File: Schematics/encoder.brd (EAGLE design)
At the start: 100 x 80 mm, 2 parts, among them U1 ENCODER_2LED

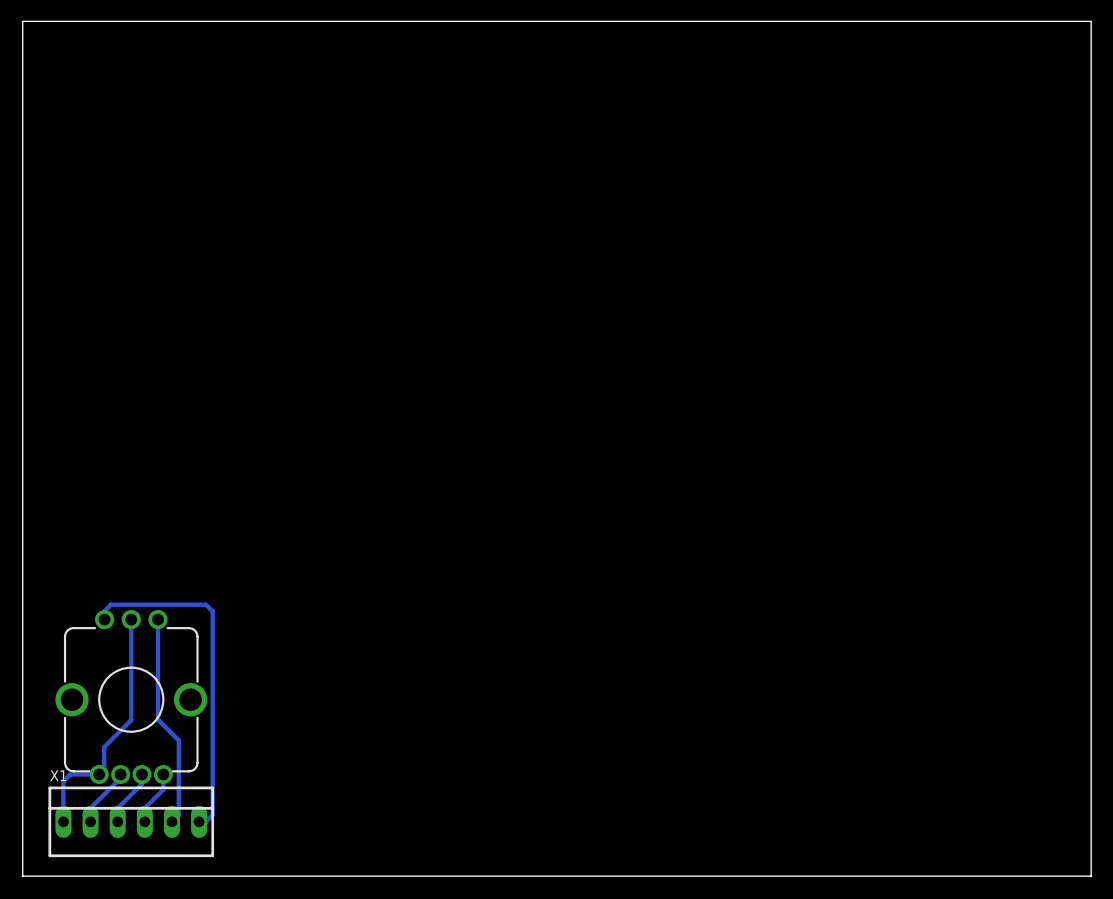
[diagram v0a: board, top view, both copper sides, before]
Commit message: Add caps to encoder breakout
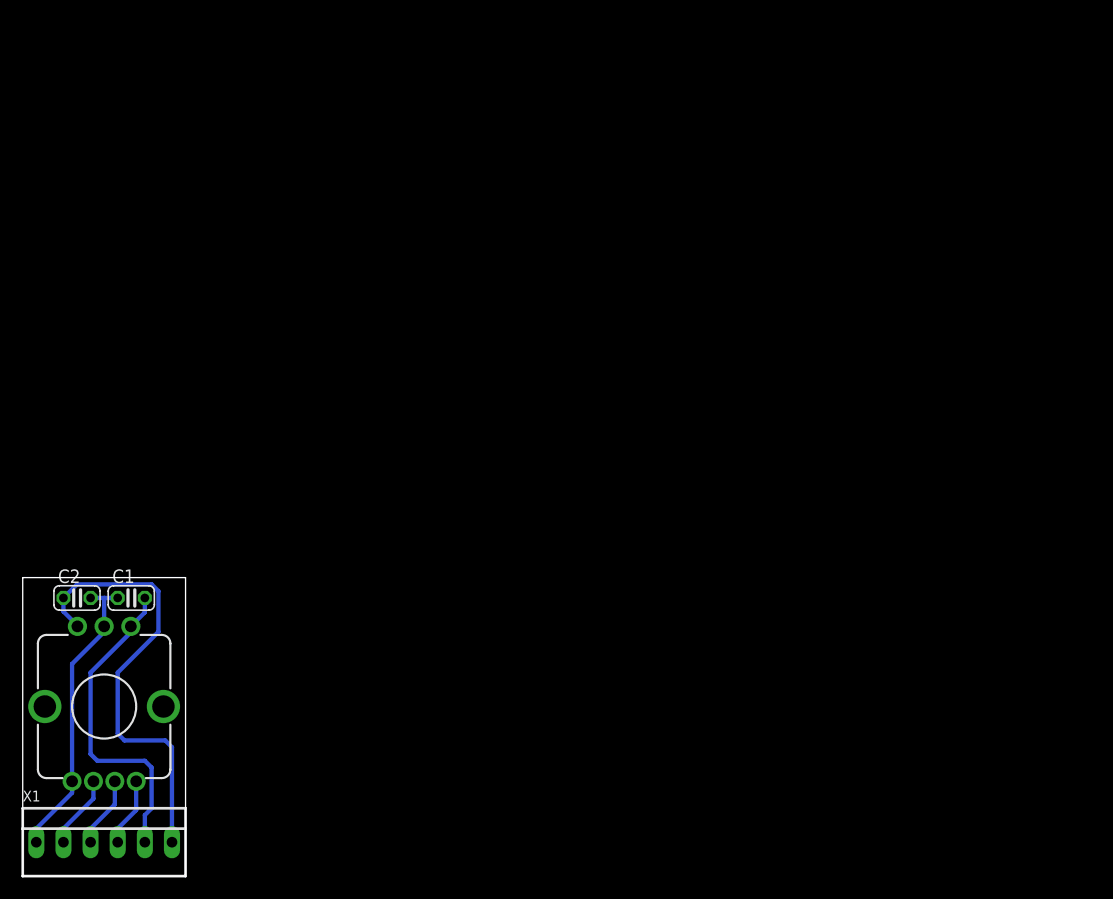
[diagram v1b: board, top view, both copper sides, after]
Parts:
- added C1, C2: (no value), rcl:C025-024X044
- moved X1 3.17 mm to (7.62, 3.17)
- moved U1 2.62 mm to (7.62, 15.9)
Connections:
- removed net N$1: U1.C, U1.GND, X1.1
- new net GND: C1.1, C2.2, U1.C, U1.GND, X1.1
- net N$5: now also C1.2
- net N$6: now also C2.1
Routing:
- net GND: track 0.00 -> 28.0 mm
- net N$1: track 23.2 -> 0.00 mm
- net N$6: track 32.0 -> 42.3 mm
- net N$5: track 20.0 -> 30.2 mm
- net N$3: track 5.37 -> 6.64 mm
- net N$2: track 5.59 -> 6.86 mm
- net N$4: track 5.15 -> 6.42 mm
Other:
- board size 100 x 80 mm -> 15.2 x 27.9 mm
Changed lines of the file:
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@@
 <board>
 <plain>
-<wire x1="0" y1="0" x2="100" y2="0" width="0" layer="20"/>
-<wire x1="100" y1="0" x2="100" y2="80" width="0" layer="20"/>
-<wire x1="100" y1="80" x2="0" y2="80" width="0" layer="20"/>
-<wire x1="0" y1="80" x2="0" y2="0" width="0" layer="20"/>
+<wire x1="0" y1="0" x2="15.24" y2="0" width="0" layer="20"/>
+<wire x1="15.24" y1="0" x2="15.24" y2="27.94" width="0" layer="20"/>
+<wire x1="15.24" y1="27.94" x2="0" y2="27.94" width="0" layer="20"/>
+<wire x1="0" y1="27.94" x2="0" y2="0" width="0" layer="20"/>
 </plain>
 <attributes>
@@
 </autorouter>
 <elements>
-<element name="U1" library="SparkFun" package="ENCODER_LED_2" value="ENCODER_2LED" x="10.16" y="16.51" rot="R180"/>
-<element name="X1" library="con-molex" package="22-23-2061" value="" x="10.16" y="5.08">
-<attribute name="OC_NEWARK" value="27C1933" x="31.75" y="-15.24" size="1.778" layer="27" display="off"/>
-<attribute name="MPN" value="22-23-2061" x="31.75" y="-15.24" size="1.778" layer="27" display="off"/>
-<attribute name="MF" value="MOLEX" x="31.75" y="-15.24" size="1.778" layer="27" display="off"/>
-<attribute name="OC_FARNELL" value="1462922" x="31.75" y="-15.24" size="1.778" layer="27" display="off"/>
+<element name="U1" library="SparkFun" package="ENCODER_LED_2" value="ENCODER_2LED" x="7.62" y="15.875" rot="R180"/>
+<element name="X1" library="con-molex" package="22-23-2061" value="" x="7.62" y="3.175">
+<attribute name="OC_NEWARK" value="27C1933" x="29.21" y="-17.145" size="1.778" layer="27" display="off"/>
+<attribute name="MPN" value="22-23-2061" x="29.21" y="-17.145" size="1.778" layer="27" display="off"/>
+<attribute name="MF" value="MOLEX" x="29.21" y="-17.145" size="1.778" layer="27" display="off"/>
+<attribute name="OC_FARNELL" value="1462922" x="29.21" y="-17.145" size="1.778" layer="27" display="off"/>
 </element>
+<element name="C1" library="rcl" package="C025-024X044" value="" x="10.16" y="26.035"/>
+<element name="C2" library="rcl" package="C025-024X044" value="" x="5.08" y="26.035"/>
 </elements>
 <signals>
@@
 <contactref element="U1" pad="+G"/>
 <contactref element="X1" pad="2"/>
-<wire x1="9.16" y1="9.51" x2="9.16" y2="9.16" width="0.4064" layer="16"/>
-<wire x1="9.16" y1="9.16" x2="6.35" y2="6.35" width="0.4064" layer="16"/>
-<wire x1="6.35" y1="6.35" x2="6.35" y2="5.08" width="0.4064" layer="16"/>
+<wire x1="6.62" y1="8.875" x2="6.62" y2="7.255" width="0.4064" layer="16"/>
+<wire x1="6.62" y1="7.255" x2="3.81" y2="4.445" width="0.4064" layer="16"/>
+<wire x1="3.81" y1="4.445" x2="3.81" y2="3.175" width="0.4064" layer="16"/>
 </signal>
 <signal name="N$3">
 <contactref element="U1" pad="+R"/>
 <contactref element="X1" pad="3"/>
-<wire x1="11.16" y1="9.51" x2="11.16" y2="8.62" width="0.4064" layer="16"/>
-<wire x1="11.16" y1="8.62" x2="8.89" y2="6.35" width="0.4064" layer="16"/>
-<wire x1="8.89" y1="6.35" x2="8.89" y2="5.08" width="0.4064" layer="16"/>
+<wire x1="8.62" y1="8.875" x2="8.62" y2="6.715" width="0.4064" layer="16"/>
+<wire x1="8.62" y1="6.715" x2="6.35" y2="4.445" width="0.4064" layer="16"/>
+<wire x1="6.35" y1="4.445" x2="6.35" y2="3.175" width="0.4064" layer="16"/>
 </signal>
 <signal name="N$4">
 <contactref element="U1" pad="SW"/>
 <contactref element="X1" pad="4"/>
-<wire x1="13.16" y1="9.51" x2="13.16" y2="8.08" width="0.4064" layer="16"/>
-<wire x1="13.16" y1="8.08" x2="11.43" y2="6.35" width="0.4064" layer="16"/>
-<wire x1="11.43" y1="6.35" x2="11.43" y2="5.08" width="0.4064" layer="16"/>
+<wire x1="10.62" y1="8.875" x2="10.62" y2="6.175" width="0.4064" layer="16"/>
+<wire x1="10.62" y1="6.175" x2="8.89" y2="4.445" width="0.4064" layer="16"/>
+<wire x1="8.89" y1="4.445" x2="8.89" y2="3.175" width="0.4064" layer="16"/>
 </signal>
 <signal name="N$5">
 <contactref element="U1" pad="A"/>
 <contactref element="X1" pad="5"/>
-<wire x1="12.66" y1="24.01" x2="12.66" y2="14.645" width="0.4064" layer="16"/>
-<wire x1="12.66" y1="14.645" x2="14.605" y2="12.7" width="0.4064" layer="16"/>
-<wire x1="14.605" y1="12.7" x2="14.605" y2="5.715" width="0.4064" layer="16"/>
-<wire x1="14.605" y1="5.715" x2="13.97" y2="5.08" width="0.4064" layer="16"/>
+<contactref element="C1" pad="2"/>
+<wire x1="11.43" y1="24.685" x2="11.43" y2="26.035" width="0.4064" layer="16"/>
+<wire x1="11.43" y1="3.175" x2="11.43" y2="5.715" width="0.4064" layer="16"/>
+<wire x1="11.43" y1="5.715" x2="12.065" y2="6.35" width="0.4064" layer="16"/>
+<wire x1="12.065" y1="6.35" x2="12.065" y2="10.16" width="0.4064" layer="16"/>
+<wire x1="12.065" y1="10.16" x2="11.43" y2="10.795" width="0.4064" layer="16"/>
+<wire x1="11.43" y1="10.795" x2="6.985" y2="10.795" width="0.4064" layer="16"/>
+<wire x1="6.985" y1="10.795" x2="6.35" y2="11.43" width="0.4064" layer="16"/>
+<wire x1="6.35" y1="11.43" x2="6.35" y2="19.05" width="0.4064" layer="16"/>
+<wire x1="11.43" y1="24.685" x2="10.12" y2="23.375" width="0.4064" layer="16"/>
+<wire x1="10.12" y1="23.375" x2="10.12" y2="22.82" width="0.4064" layer="16"/>
+<wire x1="10.12" y1="22.82" x2="6.35" y2="19.05" width="0.4064" layer="16"/>
 </signal>
 <signal name="N$6">
 <contactref element="U1" pad="B"/>
 <contactref element="X1" pad="6"/>
-<wire x1="7.66" y1="24.01" x2="7.62" y2="24.05" width="0.4064" layer="16"/>
-<wire x1="7.62" y1="24.05" x2="7.62" y2="24.765" width="0.4064" layer="16"/>
-<wire x1="7.62" y1="24.765" x2="8.255" y2="25.4" width="0.4064" layer="16"/>
-<wire x1="8.255" y1="25.4" x2="17.145" y2="25.4" width="0.4064" layer="16"/>
-<wire x1="17.145" y1="25.4" x2="17.78" y2="24.765" width="0.4064" layer="16"/>
-<wire x1="17.78" y1="24.765" x2="17.78" y2="5.715" width="0.4064" layer="16"/>
-<wire x1="17.78" y1="5.715" x2="17.145" y2="5.08" width="0.4064" layer="16"/>
-<wire x1="17.145" y1="5.08" x2="16.51" y2="5.08" width="0.4064" layer="16"/>
-</signal>
-<signal name="N$1">
+<contactref element="C2" pad="1"/>
+<wire x1="5.12" y1="23.375" x2="5.12" y2="23.455" width="0.4064" layer="16"/>
+<wire x1="5.12" y1="23.455" x2="3.81" y2="24.765" width="0.4064" layer="16"/>
+<wire x1="3.81" y1="24.765" x2="3.81" y2="26.035" width="0.4064" layer="16"/>
+<wire x1="3.81" y1="26.035" x2="5.08" y2="27.305" width="0.4064" layer="16"/>
+<wire x1="9.525" y1="12.7" x2="13.335" y2="12.7" width="0.4064" layer="16"/>
+<wire x1="13.335" y1="12.7" x2="13.97" y2="12.065" width="0.4064" layer="16"/>
+<wire x1="13.97" y1="12.065" x2="13.97" y2="3.175" width="0.4064" layer="16"/>
+<wire x1="5.08" y1="27.305" x2="12.065" y2="27.305" width="0.4064" layer="16"/>
+<wire x1="12.065" y1="27.305" x2="12.7" y2="26.67" width="0.4064" layer="16"/>
+<wire x1="12.7" y1="26.67" x2="12.7" y2="22.86" width="0.4064" layer="16"/>
+<wire x1="12.7" y1="22.86" x2="8.89" y2="19.05" width="0.4064" layer="16"/>
+<wire x1="8.89" y1="19.05" x2="8.89" y2="13.335" width="0.4064" layer="16"/>
+<wire x1="8.89" y1="13.335" x2="9.525" y2="12.7" width="0.4064" layer="16"/>
+</signal>
+<signal name="GND">
+<contactref element="C2" pad="2"/>
 <contactref element="U1" pad="C"/>
 <contactref element="U1" pad="GND"/>
 <contactref element="X1" pad="1"/>
-<wire x1="7.16" y1="9.51" x2="4.445" y2="9.51" width="0.4064" layer="16"/>
-<wire x1="4.445" y1="9.51" x2="3.81" y2="8.875" width="0.4064" layer="16"/>
-<wire x1="3.81" y1="8.875" x2="3.81" y2="5.08" width="0.4064" layer="16"/>
-<wire x1="7.16" y1="9.51" x2="7.62" y2="9.97" width="0.4064" layer="16"/>
-<wire x1="7.62" y1="9.97" x2="7.62" y2="12.065" width="0.4064" layer="16"/>
-<wire x1="7.62" y1="12.065" x2="10.16" y2="14.605" width="0.4064" layer="16"/>
-<wire x1="10.16" y1="14.605" x2="10.16" y2="24.01" width="0.4064" layer="16"/>
+<contactref element="C1" pad="1"/>
+<wire x1="8.89" y1="26.035" x2="7.62" y2="26.035" width="0.4064" layer="16"/>
+<wire x1="7.62" y1="26.035" x2="6.35" y2="26.035" width="0.4064" layer="16"/>
+<wire x1="7.62" y1="23.375" x2="7.62" y2="26.035" width="0.4064" layer="16"/>
+<wire x1="7.62" y1="23.375" x2="7.62" y2="22.86" width="0.4064" layer="16"/>
+<wire x1="7.62" y1="22.86" x2="4.62" y2="19.86" width="0.4064" layer="16"/>
+<wire x1="4.62" y1="8.875" x2="4.62" y2="19.86" width="0.4064" layer="16"/>
+<wire x1="4.62" y1="8.875" x2="4.62" y2="7.795" width="0.4064" layer="16"/>
+<wire x1="4.62" y1="7.795" x2="1.27" y2="4.445" width="0.4064" layer="16"/>
+<wire x1="1.27" y1="4.445" x2="1.27" y2="3.175" width="0.4064" layer="16"/>
 </signal>
 </signals>

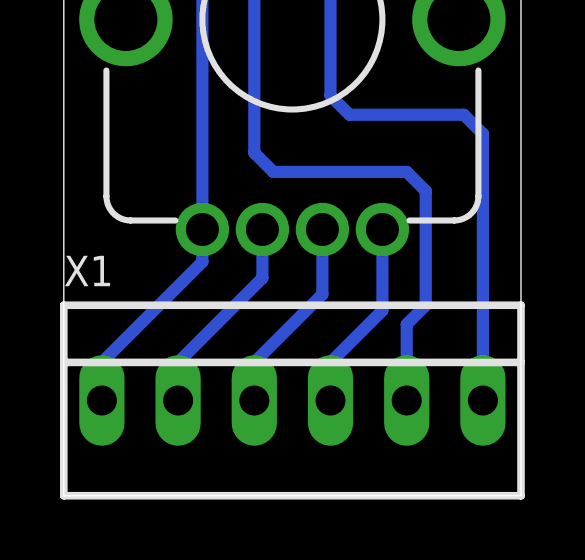
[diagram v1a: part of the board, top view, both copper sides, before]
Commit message: Add current limiting resistors for LEDs
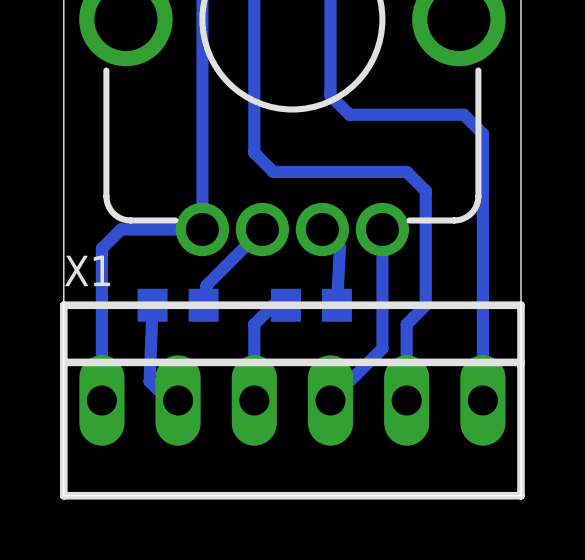
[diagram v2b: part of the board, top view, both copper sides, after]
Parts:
- added R1, R2: (no value), rcl:R0603
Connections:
- new net N$1: R1.2, X1.2
- new net N$7: R2.1, U1.+R
- net N$2: now also R2.2, X1.3; no longer U1.+G, X1.2
- net N$3: now also R1.1, U1.+G; no longer U1.+R, X1.3
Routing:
- net N$1: track 0.00 -> 3.75 mm
- net N$3: track 6.64 -> 3.30 mm
- net N$2: track 6.86 -> 3.86 mm
- net N$7: track 0.00 -> 2.77 mm
- net GND: track 28.0 -> 29.6 mm
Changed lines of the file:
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@@
 <element name="C1" library="rcl" package="C025-024X044" value="" x="10.16" y="26.035"/>
 <element name="C2" library="rcl" package="C025-024X044" value="" x="5.08" y="26.035"/>
+<element name="R1" library="rcl" package="R0603" value="" x="3.81" y="6.35" rot="MR0"/>
+<element name="R2" library="rcl" package="R0603" value="" x="8.255" y="6.35" rot="MR0"/>
 </elements>
 <signals>
-<signal name="N$2">
-<contactref element="U1" pad="+G"/>
-<contactref element="X1" pad="2"/>
-<wire x1="6.62" y1="8.875" x2="6.62" y2="7.255" width="0.4064" layer="16"/>
-<wire x1="6.62" y1="7.255" x2="3.81" y2="4.445" width="0.4064" layer="16"/>
-<wire x1="3.81" y1="4.445" x2="3.81" y2="3.175" width="0.4064" layer="16"/>
-</signal>
-<signal name="N$3">
-<contactref element="U1" pad="+R"/>
-<contactref element="X1" pad="3"/>
-<wire x1="8.62" y1="8.875" x2="8.62" y2="6.715" width="0.4064" layer="16"/>
-<wire x1="8.62" y1="6.715" x2="6.35" y2="4.445" width="0.4064" layer="16"/>
-<wire x1="6.35" y1="4.445" x2="6.35" y2="3.175" width="0.4064" layer="16"/>
-</signal>
 <signal name="N$4">
 <contactref element="U1" pad="SW"/>
 <contactref element="X1" pad="4"/>
-<wire x1="10.62" y1="8.875" x2="10.62" y2="6.175" width="0.4064" layer="16"/>
-<wire x1="10.62" y1="6.175" x2="8.89" y2="4.445" width="0.4064" layer="16"/>
-<wire x1="8.89" y1="4.445" x2="8.89" y2="3.175" width="0.4064" layer="16"/>
+<wire x1="10.62" y1="8.875" x2="10.62" y2="4.905" width="0.4064" layer="16"/>
+<wire x1="10.62" y1="4.905" x2="8.89" y2="3.175" width="0.4064" layer="16"/>
 </signal>
 <signal name="N$5">
@@
 <wire x1="7.62" y1="22.86" x2="4.62" y2="19.86" width="0.4064" layer="16"/>
 <wire x1="4.62" y1="8.875" x2="4.62" y2="19.86" width="0.4064" layer="16"/>
-<wire x1="4.62" y1="8.875" x2="4.62" y2="7.795" width="0.4064" layer="16"/>
-<wire x1="4.62" y1="7.795" x2="1.27" y2="4.445" width="0.4064" layer="16"/>
-<wire x1="1.27" y1="4.445" x2="1.27" y2="3.175" width="0.4064" layer="16"/>
+<wire x1="1.27" y1="3.175" x2="1.27" y2="8.24" width="0.4064" layer="16"/>
+<wire x1="1.27" y1="8.24" x2="1.905" y2="8.875" width="0.4064" layer="16"/>
+<wire x1="1.905" y1="8.875" x2="4.62" y2="8.875" width="0.4064" layer="16"/>
+</signal>
+<signal name="N$1">
+<contactref element="X1" pad="2"/>
+<contactref element="R1" pad="2"/>
+<wire x1="2.96" y1="6.35" x2="2.86" y2="3.81" width="0.4064" layer="16"/>
+<wire x1="2.86" y1="3.81" x2="3.495" y2="3.175" width="0.4064" layer="16"/>
+<wire x1="3.495" y1="3.175" x2="3.81" y2="3.175" width="0.4064" layer="16"/>
+</signal>
+<signal name="N$2">
+<contactref element="X1" pad="3"/>
+<contactref element="R2" pad="2"/>
+<wire x1="6.35" y1="3.175" x2="6.35" y2="5.715" width="0.4064" layer="16"/>
+<wire x1="6.35" y1="5.715" x2="6.985" y2="6.35" width="0.4064" layer="16"/>
+<wire x1="6.985" y1="6.35" x2="7.405" y2="6.35" width="0.4064" layer="16"/>
+</signal>
+<signal name="N$3">
+<contactref element="U1" pad="+G"/>
+<contactref element="R1" pad="1"/>
+<wire x1="4.66" y1="6.35" x2="4.76" y2="7.015" width="0.4064" layer="16"/>
+<wire x1="4.76" y1="7.015" x2="6.62" y2="8.875" width="0.4064" layer="16"/>
+</signal>
+<signal name="N$7">
+<contactref element="R2" pad="1"/>
+<contactref element="U1" pad="+R"/>
+<wire x1="9.105" y1="6.35" x2="9.205" y2="8.29" width="0.4064" layer="16"/>
+<wire x1="9.205" y1="8.29" x2="8.62" y2="8.875" width="0.4064" layer="16"/>
 </signal>
 </signals>

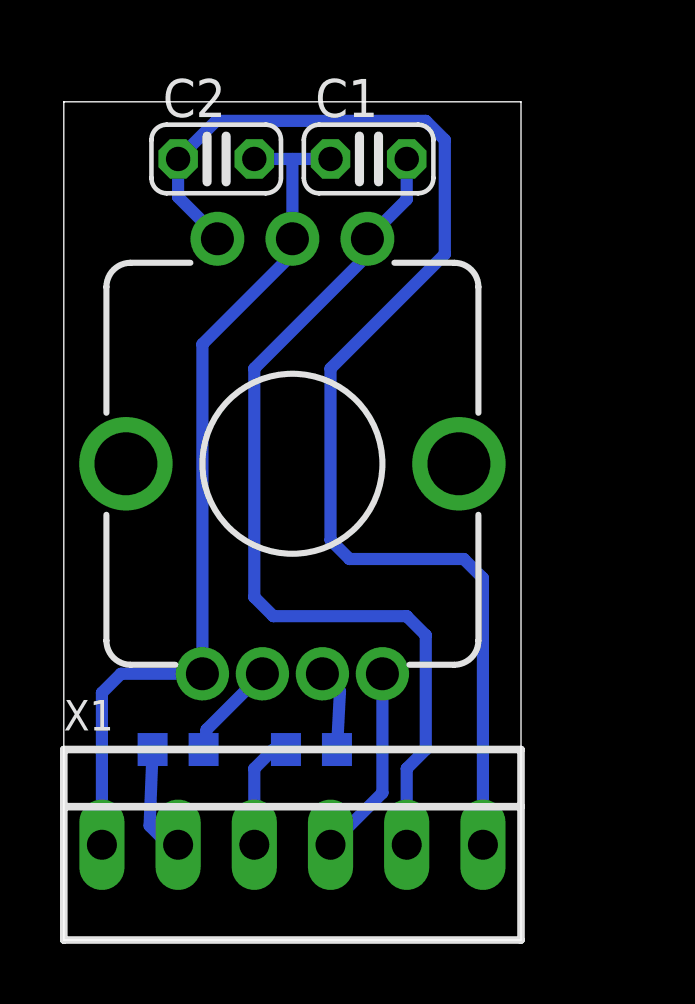
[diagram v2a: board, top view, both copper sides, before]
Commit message: bromotimer PCB: added low pass filter to encoder
Added LPF to avoid chattering, added holes to encoder pcb.
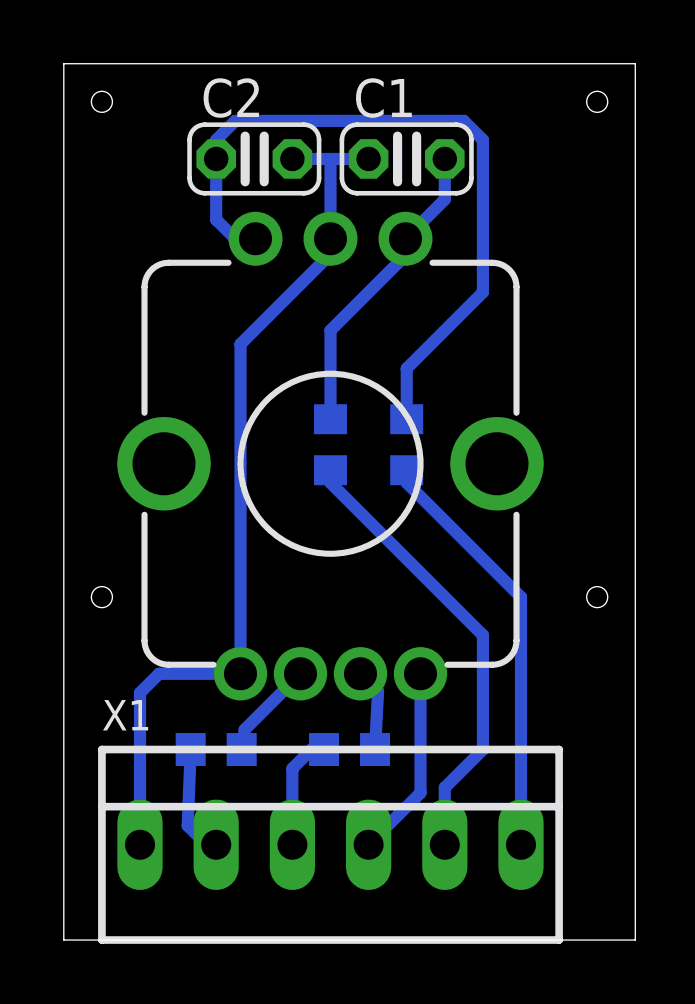
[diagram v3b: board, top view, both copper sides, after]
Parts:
- added R3, R4: 10k, rcl:R0603
- C1, C2: value (none) -> 10n
- moved U1 1.27 mm to (8.89, 15.9)
- moved X1 1.27 mm to (8.89, 3.17)
- moved R1 1.27 mm to (5.08, 6.35)
- moved C1 1.27 mm to (11.4, 26.0)
- moved C2 1.27 mm to (6.35, 26.0)
- moved R2 1.27 mm to (9.53, 6.35)
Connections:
- new net N$8: R4.1, X1.6
- new net N$9: R3.1, X1.5
- net N$5: now also R3.2; no longer X1.5
- net N$6: now also R4.2; no longer X1.6
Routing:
- net N$5: track 30.2 -> 10.3 mm
- net N$6: track 42.3 -> 24.0 mm
- net N$9: track 0.00 -> 15.1 mm
- net N$8: track 0.00 -> 14.1 mm
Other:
- board size 15.2 x 27.9 mm -> 19.1 x 29.2 mm
